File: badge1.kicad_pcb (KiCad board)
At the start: 2 copper layers, 50 x 99.9 mm, 21 parts, among them P1 CONN_01X04, P2 USB_A, P3 CONN_01X04, SW1 SW_PUSH, U1 badge_hole, U2 custom_logo, U3 Hillhacks_logo, U4 proto_area

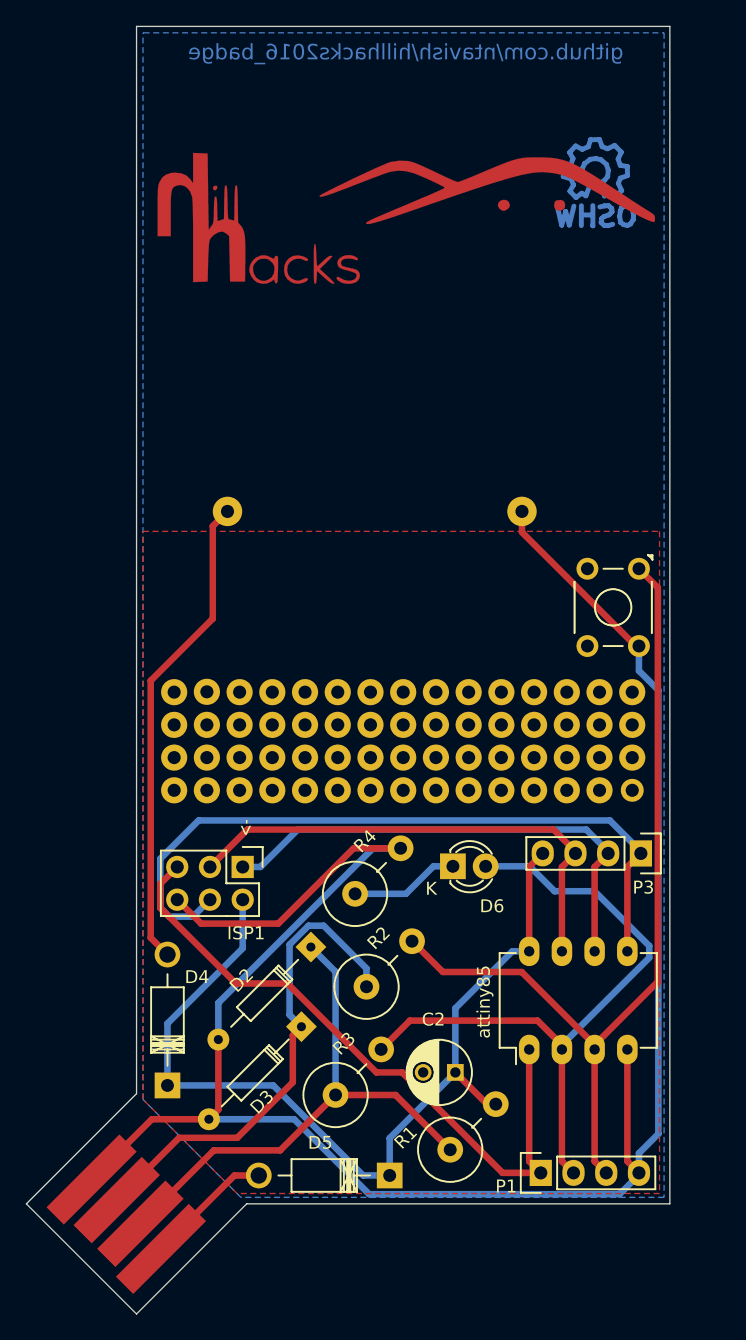
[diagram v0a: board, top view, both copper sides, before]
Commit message: Updated with @anool's comments.
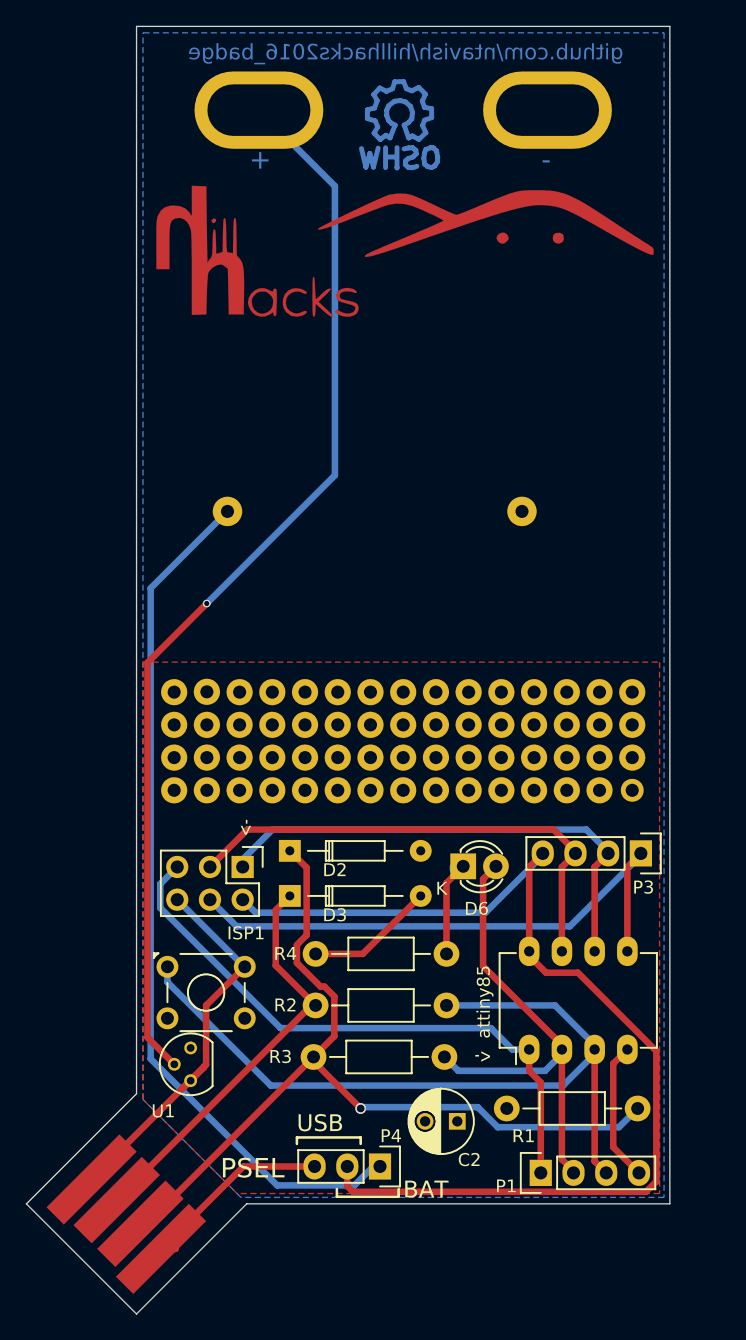
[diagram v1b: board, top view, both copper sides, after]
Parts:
- removed D4, D5: 1N5817, Diodes_ThroughHole:Diode_DO-41_SOD81_Horizontal_RM10
- added P4: CONN_01X03, Pin_Headers:Pin_Header_Straight_1x03, F.Cu at (147.5, 128.5)
- added U5: badge_hole2, badge_mod:badge_hole_6mmx3mm(+2mmCu), F.Cu at (138.1, 46.5)
- added U6: badge_hole2, badge_mod:badge_hole_6mmx3mm(+2mmCu), F.Cu at (160.5, 46.5)
- R1, R2, R3, R4: footprint Resistors_ThroughHole:Resistor_Vertical_RM5mm -> Resistors_ThroughHole:Resistor_Horizontal_RM10mm
- U1: value badge_hole -> MCP1700-3302E/TO; footprint badge_mod:badge_hole_6mmx3mm -> TO_SOT_Packages_THT:TO-92_Molded_Narrow
- moved U1 77.8 mm to (132.8, 121.8), turned to 90 degrees
- moved SW1 47.9 mm to (131.0, 113.0), turned to 0 degrees
- moved U2 15.9 mm to (148.3, 47.0)
- moved R1 12.9 mm to (167.5, 124.0), turned to 180 degrees
- moved D3 10.2 mm to (140.5, 107.5), turned to 0 degrees
- moved R4 8.35 mm to (152.7, 112.0), turned to 180 degrees
- moved D2 7.64 mm to (140.5, 104.0), turned to 0 degrees
- moved R2 6.56 mm to (142.5, 116.0), turned to 0 degrees
- moved C2 3.80 mm to (153.5, 125.0)
- moved R3 3.67 mm to (142.3, 120.0), turned to 0 degrees
- moved U3 2.55 mm to (149.2, 57.8)
- moved D6 0.80 mm to (154.0, 105.2)
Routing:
- net GND: track 163.4 -> 52.5 mm
- net /V_sec_bat: track 0.00 -> 86.1 mm, vias 0 -> 1
- net /VBAT: track 37.4 -> 67.6 mm
- net /USB-D-: track 42.2 -> 66.0 mm, vias 0 -> 1
- net /D3: track 52.2 -> 38.2 mm
- net VCC: track 71.8 -> 84.1 mm
- net /D0: track 56.6 -> 45.3 mm
- net /USB-D+: track 38.2 -> 31.9 mm
- net /VBUS: track 9.95 -> 15.7 mm
- net /D4: track 67.4 -> 62.5 mm
- net /RST: track 51.7 -> 47.2 mm
- net Net-(D6-Pad1): track 8.48 -> 7.63 mm
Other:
- board text added: "+"
- board text added: "-"
- board text added: "BAT"
- board text added: "PSEL"
- board text added: "USB"

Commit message: added tessearact logo. smoothed 3 corners.
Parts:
- added U7: custom_logo, badge_mod:tesseract, F.Cu at (149.2, 77.3)
- moved U2 0.40 mm to (148.8, 47.0)
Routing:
- net /V_sec_bat: track 86.1 -> 84.6 mm
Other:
- board size 50 x 99.9 mm -> 50 x 100 mm
